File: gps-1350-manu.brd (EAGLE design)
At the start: 49.9 x 34.5 mm, 59 parts, among them IC1 MSP430FR698X(1)80-PIN_PN

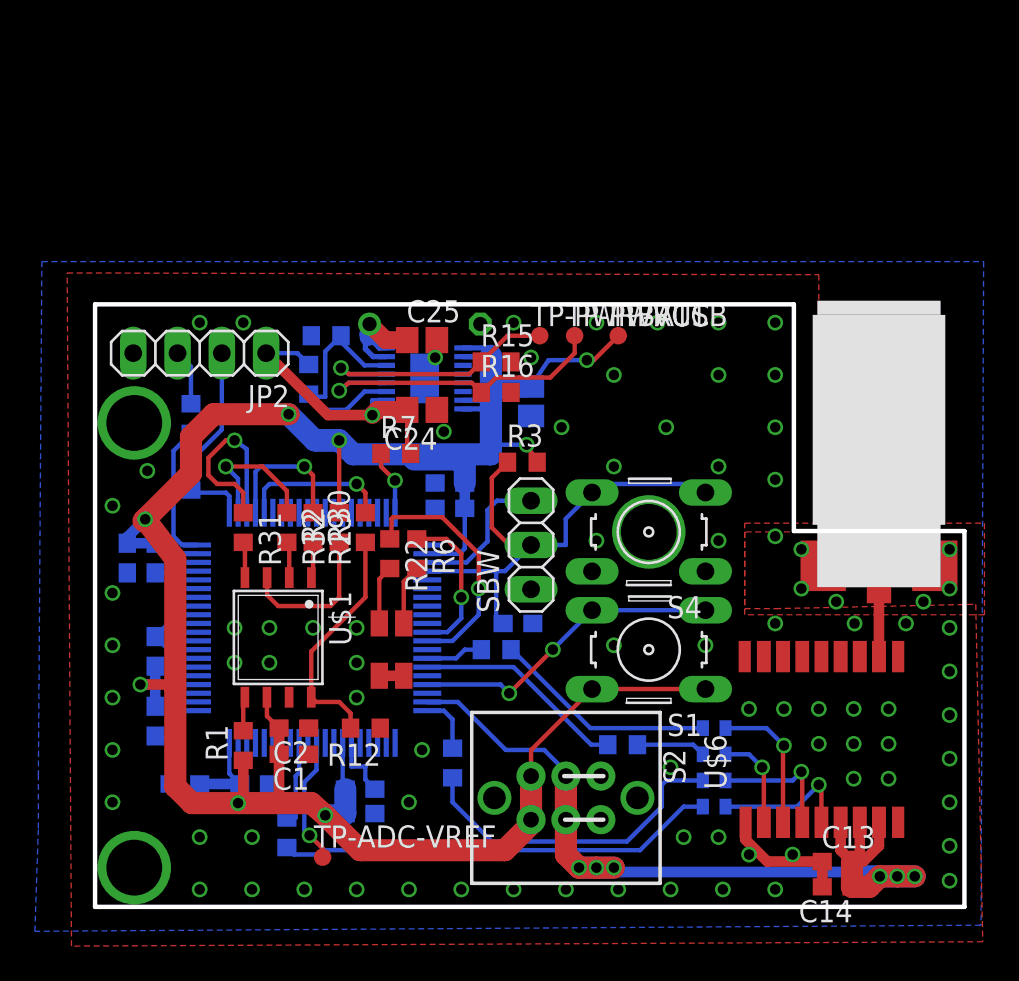
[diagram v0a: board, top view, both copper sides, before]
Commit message: Finish gps-1350-manu.brd and send it to china
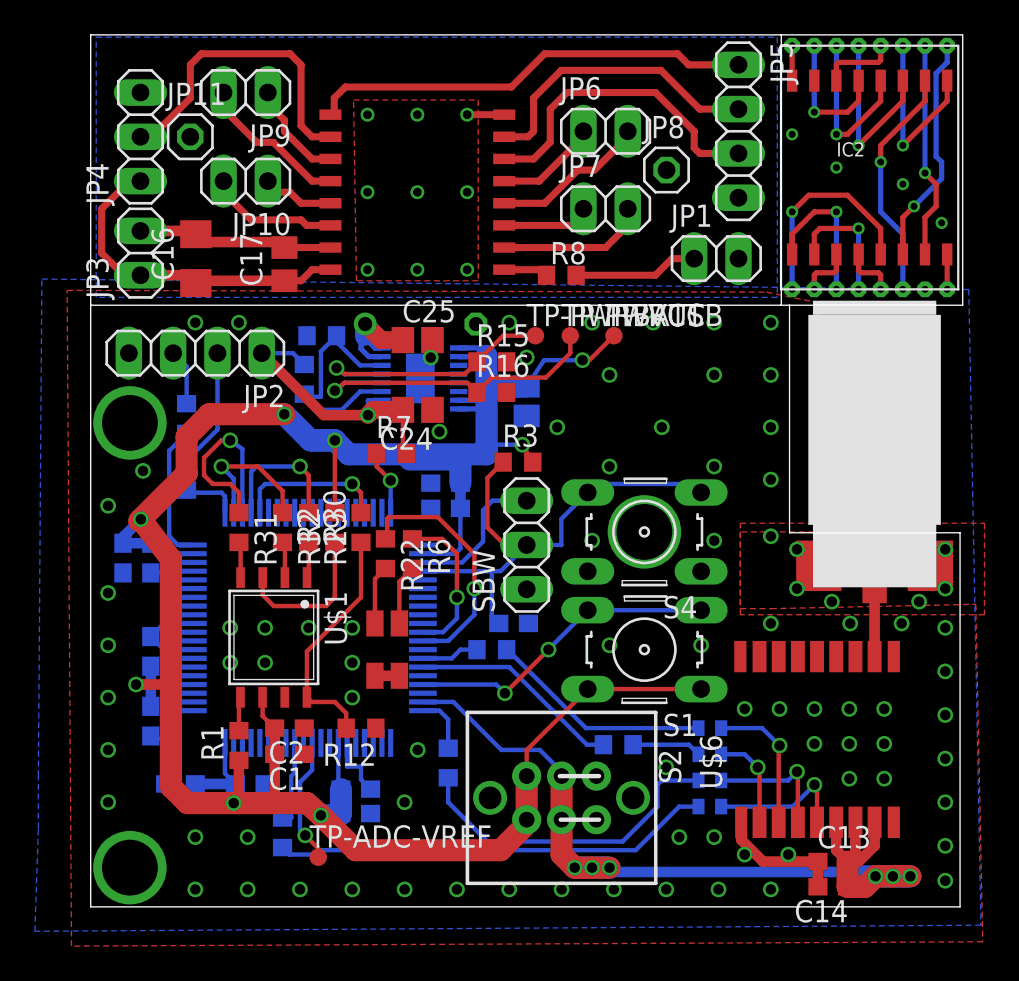
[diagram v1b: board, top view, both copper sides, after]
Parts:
- added C16: 1uF, juice:C_1206
- added C17: 100nF, juice:C_0805
- added IC2: 74HC4051ADP, juice:FLAT16-ADP
- added JP1, JP10, JP3, JP6, JP7, JP9: (no value), juice:1X02
- added JP11, JP8: (no value), pinhead:1X01
- added JP4: (no value), pinhead:1X03
- added JP5: (no value), pinhead:1X04
- added R8: (no value), juice:R_0603
- added U$3, U$4: RHD5928, juice:SO16-WS
- moved C1 0.25 mm to (11.4, 8.75)
- moved C10 0.25 mm to (3.45, 10.7)
- moved C11 0.25 mm to (5.15, 7.05)
- moved C12 0.25 mm to (9.15, 7.05)
- moved C13 0.25 mm to (42.5, 2.60)
- moved C14 0.25 mm to (42.5, 1.15)
- moved C15 0.25 mm to (24.2, 16.2)
- moved C18 0.25 mm to (25.0, 29.0)
- moved C2 0.25 mm to (11.4, 10.2)
- moved C24 0.25 mm to (18.8, 28.5)
- moved C25 0.25 mm to (18.8, 32.5)
- moved C3 0.25 mm to (3.45, 20.0)
- moved C4 0.25 mm to (1.85, 20.0)
- moved C5 0.25 mm to (15.2, 6.75)
- moved C6 0.25 mm to (15.2, 5.35)
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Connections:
- new net !EN: JP4.2, U$3.10
- new net !EN1: IC2.6, U$4.10
- new net +5V: C16.1, C17.1, JP3.1, JP4.1, U$3.16
- new net +5V1: IC2.16, U$4.16
- new net A0: JP5.1, U$3.9
- new net A1: JP5.2, U$3.7
- new net A2: JP5.3, U$3.6
- new net A3: IC2.11, U$4.9
- new net A4: IC2.10, U$4.7
- new net A5: IC2.9, U$4.6
- new net GND1: C16.2, C17.2, JP1.2, JP11.1, JP3.2, JP4.3, JP5.4, JP8.1, U$3.15, U$3.8
- new net GND2: IC2.7, IC2.8, U$4.15, U$4.8
- new net N$1: R8.1, U$3.1
- new net X: JP1.1, R8.2
- new net X0: JP9.1, U$3.11
- new net X1: JP9.2, U$3.12
- new net X10: IC2.15, U$4.13
- new net X11: IC2.12, U$4.14
- new net X12: IC2.1, U$4.5
- new net X13: IC2.5, U$4.4
- new net X14: IC2.2, U$4.3
- new net X15: IC2.4, U$4.2
- new net X16: IC2.3, U$4.1
- new net X2: JP10.1, U$3.13
- new net X3: JP10.2, U$3.14
- new net X4: JP6.1, U$3.5
- new net X5: JP6.2, U$3.4
- new net X6: JP7.1, U$3.3
- new net X7: JP7.2, U$3.2
- new net X8: IC2.13, U$4.11
- new net X9: IC2.14, U$4.12
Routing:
- net A0: track 0.00 -> 25.5 mm
- net +5V: track 0.00 -> 19.6 mm
- net A2: track 0.00 -> 18.1 mm
- net !EN: track 0.00 -> 18.0 mm
- net A1: track 0.00 -> 17.0 mm
- net !EN1: track 0.00 -> 13.5 mm, vias 0 -> 1
- net GND1: track 0.00 -> 13.4 mm, vias 0 -> 9
- net A5: track 0.00 -> 13.3 mm, vias 0 -> 1
- net A4: track 0.00 -> 12.5 mm, vias 0 -> 1
- net X12: track 0.00 -> 12.2 mm, vias 0 -> 1
- net X8: track 0.00 -> 10.5 mm, vias 0 -> 1
- net A3: track 0.00 -> 10.5 mm, vias 0 -> 1
- net X9: track 0.00 -> 9.58 mm, vias 0 -> 1
- net X5: track 0.00 -> 8.98 mm
- net X1: track 0.00 -> 8.79 mm
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- added copper zone on layer 1, net GND1
- added copper zone on layer 16, net GND1
- added copper zone on layer 1, net GND2
- added copper zone on layer 16, net GND2
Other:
- board size 49.9 x 34.5 mm -> 50 x 50 mm
- board text added: "!EN"
- board text added: "A0"
- board text added: "A1"
- board text added: "A3"
- board text added: "GND"
- board text added: "RHD5928 BB V1"
- board text added: "V+"
- board text added: "X"
- board text added: "X0"
- board text added: "X1"
- board text added: "X2"
- board text added: "X3"
- board text added: "X4"
- board text added: "X5"
- board text added: "X6"
- board text added: "X7"
